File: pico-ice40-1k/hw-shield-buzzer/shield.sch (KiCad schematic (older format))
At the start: 27 parts, among them J1 JACK_TRS_6PINS, P1 CONN_01X12, P2 CONN_01X12, P3 CONN_01X02, SW2 SW_PUSH, U1 TLV320DAC3203, U2 LD39015M18R, U3 TPA2005D1

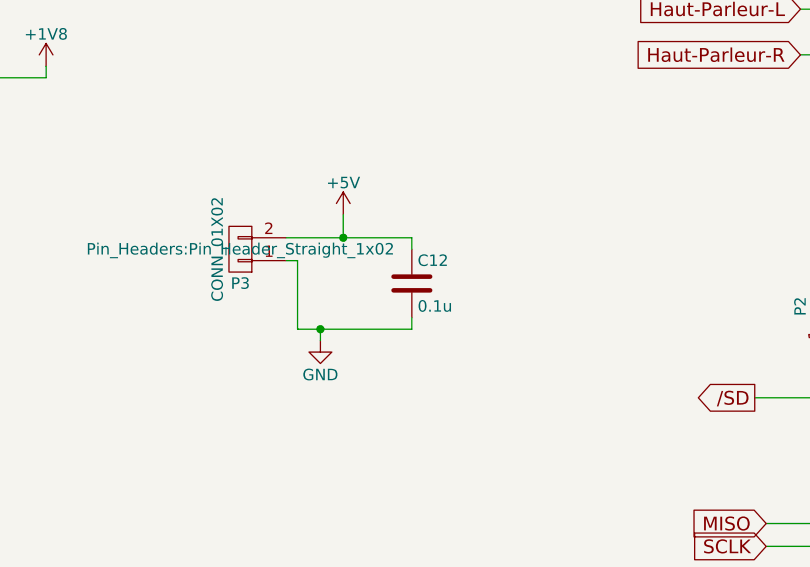
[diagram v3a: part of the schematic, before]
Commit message: update sch and pcb; add a speaker
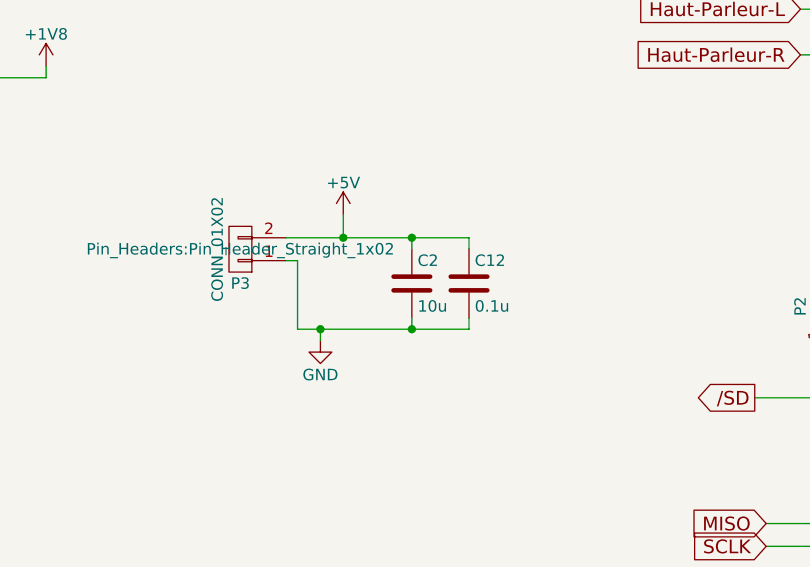
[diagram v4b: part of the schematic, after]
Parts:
- added C2: 10u, Capacitors_SMD:C_0805, symbol C
- SP1: footprint Buzzers_Beepers:BUZZER -> shield_foorprint:LOUDSPEAKER-ABS-216-RC
- U2: Fabrcant STMICROELECTRONICS -> (none); Fabricant (none) -> STMICROELECTRONICS
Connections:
- net +5V: now also C2.1
- net GND: now also C2.2
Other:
- moved on the sheet: C12
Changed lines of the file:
@@
 $EndComp
 $Comp
-L GND #PWR01
+L GND #PWR4
 U 1 1 5731BF12
 P 1350 1350
-F 0 "#PWR01" H 1350 1100 50  0001 C CNN
+F 0 "#PWR4" H 1350 1100 50  0001 C CNN
 F 1 "GND" H 1350 1200 50  0000 C CNN
 F 2 "" H 1350 1350 50  0000 C CNN
@@
 $EndComp
 $Comp
-L GND #PWR02
+L GND #PWR17
 U 1 1 5731D497
 P 7300 6000
-F 0 "#PWR02" H 7300 5750 50  0001 C CNN
+F 0 "#PWR17" H 7300 5750 50  0001 C CNN
 F 1 "GND" H 7300 5850 50  0000 C CNN
 F 2 "" H 7300 6000 50  0000 C CNN
@@
 $EndComp
 $Comp
-L +3.3V #PWR03
+L +3.3V #PWR11
 U 1 1 57328B7D
 P 3950 5100
-F 0 "#PWR03" H 3950 4950 50  0001 C CNN
+F 0 "#PWR11" H 3950 4950 50  0001 C CNN
 F 1 "+3.3V" H 3950 5240 50  0000 C CNN
 F 2 "" H 3950 5100 50  0000 C CNN
@@
 $EndComp
 $Comp
-L GND #PWR04
+L GND #PWR12
 U 1 1 57328C88
 P 4050 6400
-F 0 "#PWR04" H 4050 6150 50  0001 C CNN
+F 0 "#PWR12" H 4050 6150 50  0001 C CNN
 F 1 "GND" H 4050 6250 50  0000 C CNN
 F 2 "" H 4050 6400 50  0000 C CNN
@@
 $EndComp
 $Comp
-L GND #PWR05
+L GND #PWR26
 U 1 1 5732A695
 P 9100 4250
-F 0 "#PWR05" H 9100 4000 50  0001 C CNN
+F 0 "#PWR26" H 9100 4000 50  0001 C CNN
 F 1 "GND" H 9100 4100 50  0000 C CNN
 F 2 "" H 9100 4250 50  0000 C CNN
@@
 $EndComp
 $Comp
-L GND #PWR06
+L GND #PWR7
 U 1 1 573304E6
 P 3100 6700
-F 0 "#PWR06" H 3100 6450 50  0001 C CNN
+F 0 "#PWR7" H 3100 6450 50  0001 C CNN
 F 1 "GND" H 3100 6550 50  0000 C CNN
 F 2 "" H 3100 6700 50  0000 C CNN
@@
 MISO
 $Comp
-L GND #PWR07
+L GND #PWR15
 U 1 1 57336EFC
 P 6700 6400
-F 0 "#PWR07" H 6700 6150 50  0001 C CNN
+F 0 "#PWR15" H 6700 6150 50  0001 C CNN
 F 1 "GND" H 6700 6250 50  0000 C CNN
 F 2 "" H 6700 6400 50  0000 C CNN
@@
 $EndComp
 $Comp
-L GND #PWR08
+L GND #PWR23
 U 1 1 57337161
 P 8000 5900
-F 0 "#PWR08" H 8000 5650 50  0001 C CNN
+F 0 "#PWR23" H 8000 5650 50  0001 C CNN
 F 1 "GND" H 8000 5750 50  0000 C CNN
 F 2 "" H 8000 5900 50  0000 C CNN
@@
 $EndComp
 $Comp
-L GND #PWR09
+L GND #PWR20
 U 1 1 573371A2
 P 7450 6000
-F 0 "#PWR09" H 7450 5750 50  0001 C CNN
+F 0 "#PWR20" H 7450 5750 50  0001 C CNN
 F 1 "GND" H 7450 5850 50  0000 C CNN
 F 2 "" H 7450 6000 50  0000 C CNN
@@
 $EndComp
 $Comp
-L GND #PWR010
+L GND #PWR16
 U 1 1 573371E3
 P 7150 6000
-F 0 "#PWR010" H 7150 5750 50  0001 C CNN
+F 0 "#PWR16" H 7150 5750 50  0001 C CNN
 F 1 "GND" H 7150 5850 50  0000 C CNN
 F 2 "" H 7150 6000 50  0000 C CNN
@@
 $EndComp
 $Comp
-L +3V3 #PWR011
+L +3V3 #PWR3
 U 1 1 57338212
 P 1350 800
-F 0 "#PWR011" H 1350 650 50  0001 C CNN
+F 0 "#PWR3" H 1350 650 50  0001 C CNN
 F 1 "+3V3" H 1350 940 50  0000 C CNN
 F 2 "" H 1350 800 50  0000 C CNN
@@
 F 2 "TO_SOT_Packages_SMD:SOT-23-5" H 2200 2300 50  0000 C CIN
 F 3 "" H 2150 2000 50  0000 C CNN
-F 4 "STMICROELECTRONICS" H 2150 2000 60  0001 C CNN "Fabrcant"
+F 4 "STMICROELECTRONICS" H 2150 2000 60  0001 C CNN "Fabricant"
 F 5 "LD39015M18R" H 2150 2000 60  0001 C CNN "ref Fabricant"
 F 6 "2311332 " H 2150 2000 60  0001 C CNN "Ref Farnell"
@@
 $EndComp
 $Comp
-L +3.3V #PWR012
+L +3.3V #PWR1
 U 1 1 5733377B
 P 1000 1900
-F 0 "#PWR012" H 1000 1750 50  0001 C CNN
+F 0 "#PWR1" H 1000 1750 50  0001 C CNN
 F 1 "+3.3V" H 1000 2040 50  0000 C CNN
 F 2 "" H 1000 1900 50  0000 C CNN
@@
 $EndComp
 $Comp
-L +1V8 #PWR013
+L +1V8 #PWR10
 U 1 1 573337B9
 P 3400 1900
-F 0 "#PWR013" H 3400 1750 50  0001 C CNN
+F 0 "#PWR10" H 3400 1750 50  0001 C CNN
 F 1 "+1V8" H 3400 2040 50  0000 C CNN
 F 2 "" H 3400 1900 50  0000 C CNN
@@
 $EndComp
 $Comp
-L GND #PWR014
+L GND #PWR2
 U 1 1 57334A7B
 P 1250 2350
-F 0 "#PWR014" H 1250 2100 50  0001 C CNN
+F 0 "#PWR2" H 1250 2100 50  0001 C CNN
 F 1 "GND" H 1250 2200 50  0000 C CNN
 F 2 "" H 1250 2350 50  0000 C CNN
@@
 $EndComp
 $Comp
-L GND #PWR015
+L GND #PWR5
 U 1 1 57334BD9
 P 2150 2400
-F 0 "#PWR015" H 2150 2150 50  0001 C CNN
+F 0 "#PWR5" H 2150 2150 50  0001 C CNN
 F 1 "GND" H 2150 2250 50  0000 C CNN
 F 2 "" H 2150 2400 50  0000 C CNN
@@
 $EndComp
 $Comp
-L GND #PWR016
+L GND #PWR6
 U 1 1 573357A1
 P 2900 2400
-F 0 "#PWR016" H 2900 2150 50  0001 C CNN
+F 0 "#PWR6" H 2900 2150 50  0001 C CNN
 F 1 "GND" H 2900 2250 50  0000 C CNN
 F 2 "" H 2900 2400 50  0000 C CNN
@@
 $EndComp
 $Comp
-L +3.3V #PWR017
+L +3.3V #PWR18
 U 1 1 5733605F
 P 7350 3950
-F 0 "#PWR017" H 7350 3800 50  0001 C CNN
+F 0 "#PWR18" H 7350 3800 50  0001 C CNN
 F 1 "+3.3V" H 7350 4090 50  0000 C CNN
 F 2 "" H 7350 3950 50  0000 C CNN
@@
 $EndComp
 $Comp
-L +3.3V #PWR018
+L +3.3V #PWR22
 U 1 1 57336093
 P 7700 3950
-F 0 "#PWR018" H 7700 3800 50  0001 C CNN
+F 0 "#PWR22" H 7700 3800 50  0001 C CNN
 F 1 "+3.3V" H 7700 4090 50  0000 C CNN
 F 2 "" H 7700 3950 50  0000 C CNN
@@
 $EndComp
 $Comp
-L +1V8 #PWR019
+L +1V8 #PWR21
 U 1 1 573360C7
 P 7500 4050
-F 0 "#PWR019" H 7500 3900 50  0001 C CNN
+F 0 "#PWR21" H 7500 3900 50  0001 C CNN
 F 1 "+1V8" H 7500 4190 50  0000 C CNN
 F 2 "" H 7500 4050 50  0000 C CNN
 F 3 "" H 7500 4050 50  0000 C CNN
 	1    7500 4050
-	1    0    0    -1
-$EndComp
-$Comp
-L SPEAKER SP1
-U 1 1 5733A051
-P 10100 1700
-F 0 "SP1" H 10000 1950 50  0000 C CNN
-F 1 "SPEAKER" H 10000 1450 50  0000 C CNN
-F 2 "Buzzers_Beepers:BUZZER" H 10100 1700 50  0001 C CNN
-F 3 "" H 10100 1700 50  0000 C CNN
-	1    10100 1700
 	1    0    0    -1
 $EndComp
@@
 $EndComp
 $Comp
-L GND #PWR020
+L GND #PWR9
 U 1 1 573668D4
 P 3350 7150
-F 0 "#PWR020" H 3350 6900 50  0001 C CNN
+F 0 "#PWR9" H 3350 6900 50  0001 C CNN
 F 1 "GND" H 3350 7000 50  0000 C CNN
 F 2 "" H 3350 7150 50  0000 C CNN
@@
 $EndComp
 $Comp
-L +3.3V #PWR021
+L +3.3V #PWR8
 U 1 1 573B41C9
 P 3250 5550
-F 0 "#PWR021" H 3250 5400 50  0001 C CNN
+F 0 "#PWR8" H 3250 5400 50  0001 C CNN
 F 1 "+3.3V" H 3250 5690 50  0000 C CNN
 F 2 "" H 3250 5550 50  0000 C CNN
@@
 /SD
 $Comp
-L GND #PWR022
+L GND #PWR25
 U 1 1 573D0797
 P 8650 2150
-F 0 "#PWR022" H 8650 1900 50  0001 C CNN
+F 0 "#PWR25" H 8650 1900 50  0001 C CNN
 F 1 "GND" H 8650 2000 50  0000 C CNN
 F 2 "" H 8650 2150 50  0000 C CNN
@@
 $EndComp
 $Comp
-L GND #PWR023
+L GND #PWR13
 U 1 1 573D7DCD
 P 4600 3100
-F 0 "#PWR023" H 4600 2850 50  0001 C CNN
+F 0 "#PWR13" H 4600 2850 50  0001 C CNN
 F 1 "GND" H 4600 2950 50  0000 C CNN
 F 2 "" H 4600 3100 50  0000 C CNN
@@
 $EndComp
 $Comp
-L GND #PWR024
+L GND #PWR19
 U 1 1 573D96A9
 P 7450 1350
-F 0 "#PWR024" H 7450 1100 50  0001 C CNN
+F 0 "#PWR19" H 7450 1100 50  0001 C CNN
 F 1 "GND" H 7450 1200 50  0000 C CNN
 F 2 "" H 7450 1350 50  0000 C CNN
@@
 $EndComp
 $Comp
-L +5V #PWR025
+L +5V #PWR24
 U 1 1 573D9D04
 P 8650 1100
-F 0 "#PWR025" H 8650 950 50  0001 C CNN
+F 0 "#PWR24" H 8650 950 50  0001 C CNN
 F 1 "+5V" H 8650 1240 50  0000 C CNN
 F 2 "" H 8650 1100 50  0000 C CNN
@@
 L C C12
 U 1 1 573E0E9D
-P 5000 2850
-F 0 "C12" H 5025 2950 50  0000 L CNN
-F 1 "0.1u" H 5025 2750 50  0000 L CNN
-F 2 "Capacitors_SMD:C_0805" H 5038 2700 50  0001 C CNN
-F 3 "" H 5000 2850 50  0000 C CNN
-	1    5000 2850
+P 5250 2850
+F 0 "C12" H 5275 2950 50  0000 L CNN
+F 1 "0.1u" H 5275 2750 50  0000 L CNN
+F 2 "Capacitors_SMD:C_0805" H 5288 2700 50  0001 C CNN
+F 3 "" H 5250 2850 50  0000 C CNN
+	1    5250 2850
 	1    0    0    -1
 $EndComp
@@
 	4500 2750 4500 3050
 Wire Wire Line
-	4500 3050 5000 3050
+	4500 3050 5250 3050
 Wire Wire Line
 	5000 3050 5000 3000
 $Comp
-L +5V #PWR026
+L +5V #PWR14
 U 1 1 573D9873
 P 4700 2550
-F 0 "#PWR026" H 4700 2400 50  0001 C CNN
+F 0 "#PWR14" H 4700 2400 50  0001 C CNN
 F 1 "+5V" H 4700 2690 50  0000 C CNN
 F 2 "" H 4700 2550 50  0000 C CNN
@@
 	4700 2550 4700 2650
 Wire Wire Line
-	4450 2650 5000 2650
+	4450 2650 5250 2650
 Connection ~ 4700 2650
 Wire Wire Line
@@
 Wire Wire Line
 	1350 1300 2250 1300
+$Comp
+L SPEAKER SP1
+U 1 1 573DE730
+P 10100 1700
+F 0 "SP1" H 10000 1950 50  0000 C CNN
+F 1 "SPEAKER" H 10000 1450 50  0000 C CNN
+F 2 "shield_foorprint:LOUDSPEAKER-ABS-216-RC" H 10100 1700 50  0001 C CNN
+F 3 "" H 10100 1700 50  0000 C CNN
+	1    10100 1700
+	1    0    0    -1
+$EndComp
+$Comp
+L C C2
+U 1 1 573DF1BA
+P 5000 2850
+F 0 "C2" H 5025 2950 50  0000 L CNN
+F 1 "10u" H 5025 2750 50  0000 L CNN
+F 2 "Capacitors_SMD:C_0805" H 5038 2700 50  0001 C CNN
+F 3 "" H 5000 2850 50  0000 C CNN
+	1    5000 2850
+	1    0    0    -1
+$EndComp
+Wire Wire Line
+	5250 2650 5250 2700
+Connection ~ 5000 2650
+Wire Wire Line
+	5250 3050 5250 3000
+Connection ~ 5000 3050
 $EndSCHEMATC

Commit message: sch : Pull_up resistor added; Modif pcb; New files in .pretty
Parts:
- added R4, R5: 4.7k, Resistors_SMD:R_0603, symbol R
- P1, P2: value CONN_01X12 -> CONN_12; symbol CONN_01X12 -> CONN_12
- P3: symbol CONN_01X02 -> CONN_2
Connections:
- net +3V3: now also R4.1, R5.1
- net GND: now also U1.25 (PAD), U2.9 (PAD)
- net SCL: now also R4.2
- net SDA: now also R5.2
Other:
- moved on the sheet: C16, C17, C3, C4, C5, C6, J1, R2, SW2, U1
